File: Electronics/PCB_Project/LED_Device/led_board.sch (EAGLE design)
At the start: 12 parts, among them CN1 9V, IC1 7805DT, SW1 push

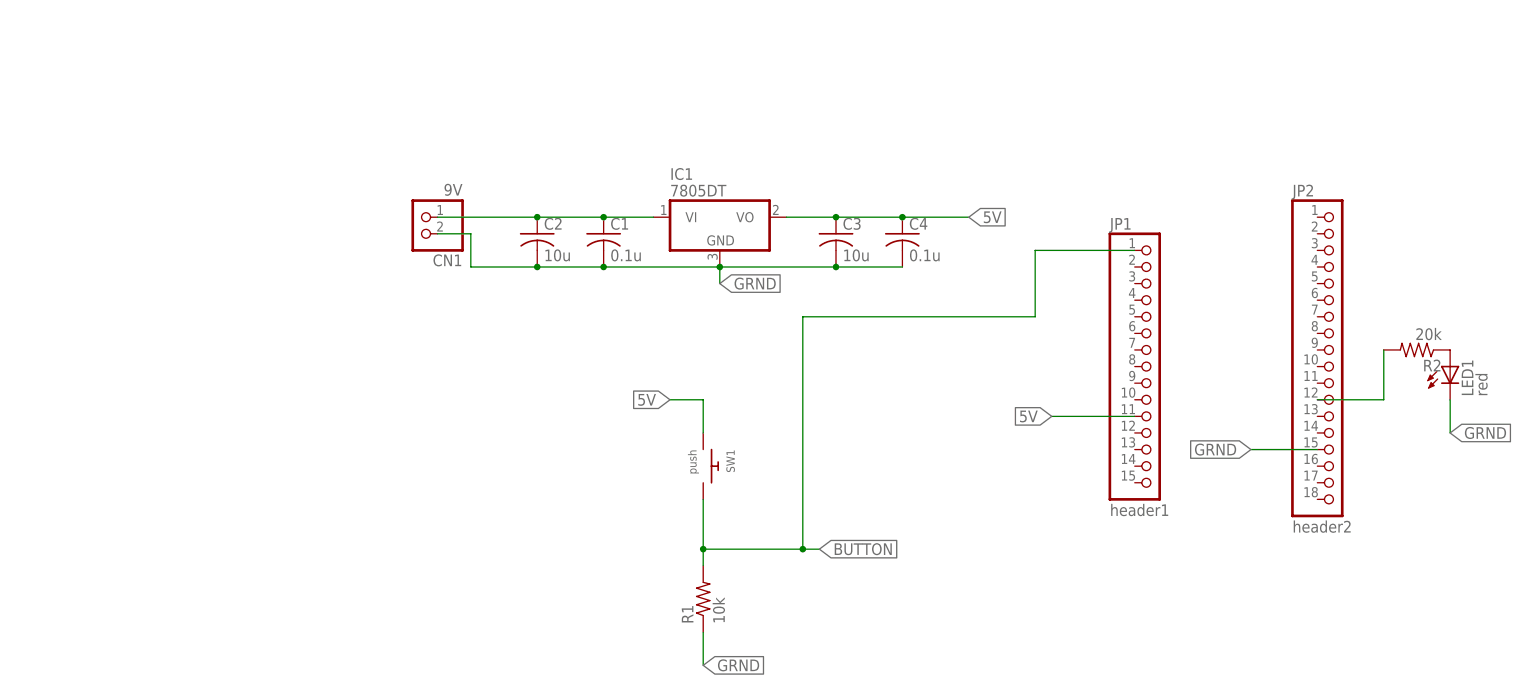
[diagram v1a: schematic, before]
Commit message: changed PCB design to have ATMEGA328 and crystal
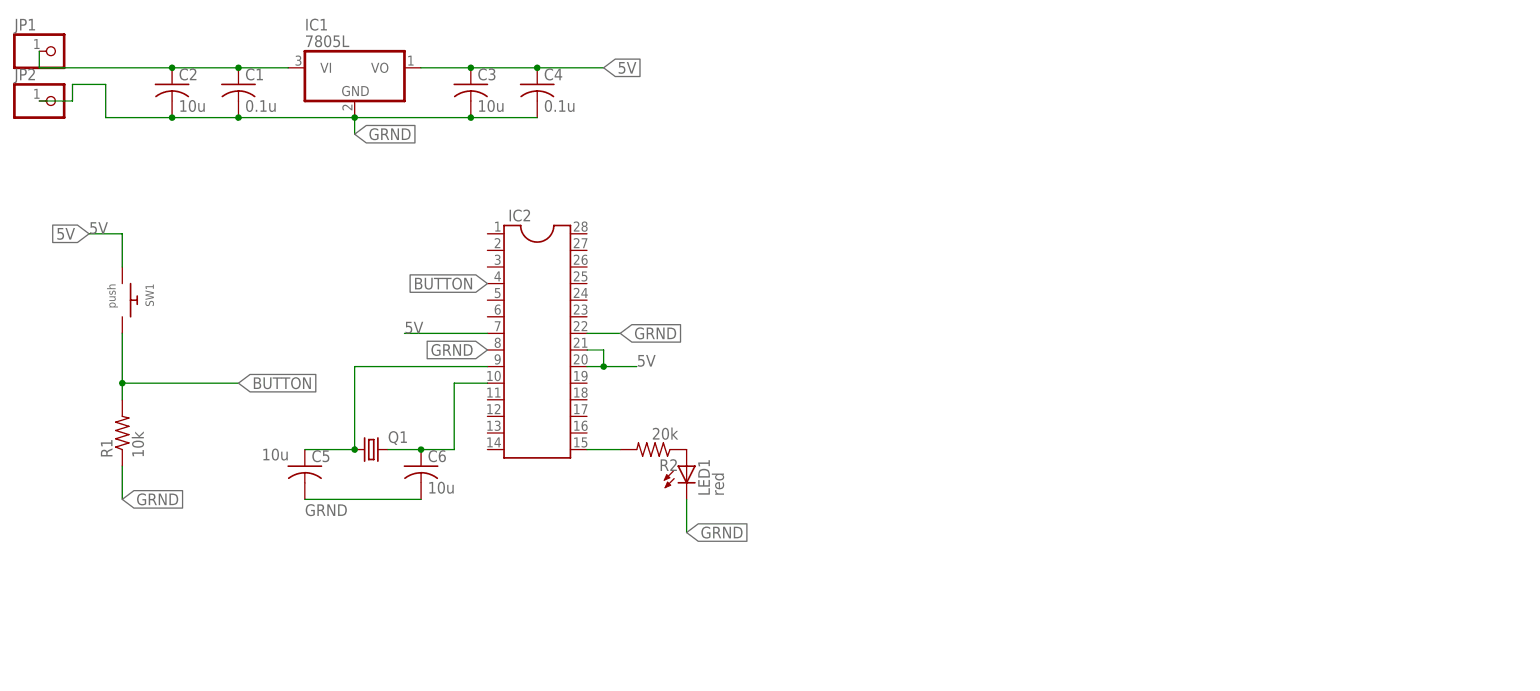
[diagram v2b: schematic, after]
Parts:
- removed CN1: 9V, adafruit:JST_2PIN-SMT
- added C5, C6: 10u, adafruit:C-USC0805
- added IC2: (no value), ic-package:DIL28
- added Q1: (no value), adafruit:CRYSTALHC49S
- IC1: value 7805DT -> 7805L; device adafruit:7805DT -> adafruit:7805L
- JP1: value header1 -> (none); device adafruit:PINHD-1X15 -> adafruit:PINHD-1X1
- JP2: value header2 -> (none); device adafruit:PINHD-1X18 -> adafruit:PINHD-1X1
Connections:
- new net N$2: IC2.22
- new net N$4: C5.1, IC2.9, Q1.1
- new net N$5: C6.1, IC2.10, Q1.2
- net 5V: now also IC2.20, IC2.21, IC2.7; no longer JP1.11
- net BUTTON: no longer JP1.1
- net GRND: now also C5.2, C6.2, JP2.1; no longer CN1.1, JP2.15
- net N$1: now also JP1.1; no longer CN1.2
- net N$7: now also IC2.15; no longer JP2.12
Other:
- moved on the sheet: C1, C2, C3, C4, IC1, LED1, R1, R2, SW1
